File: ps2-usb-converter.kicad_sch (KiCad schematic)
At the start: 1 part, among them J1 Mini-DIN-6

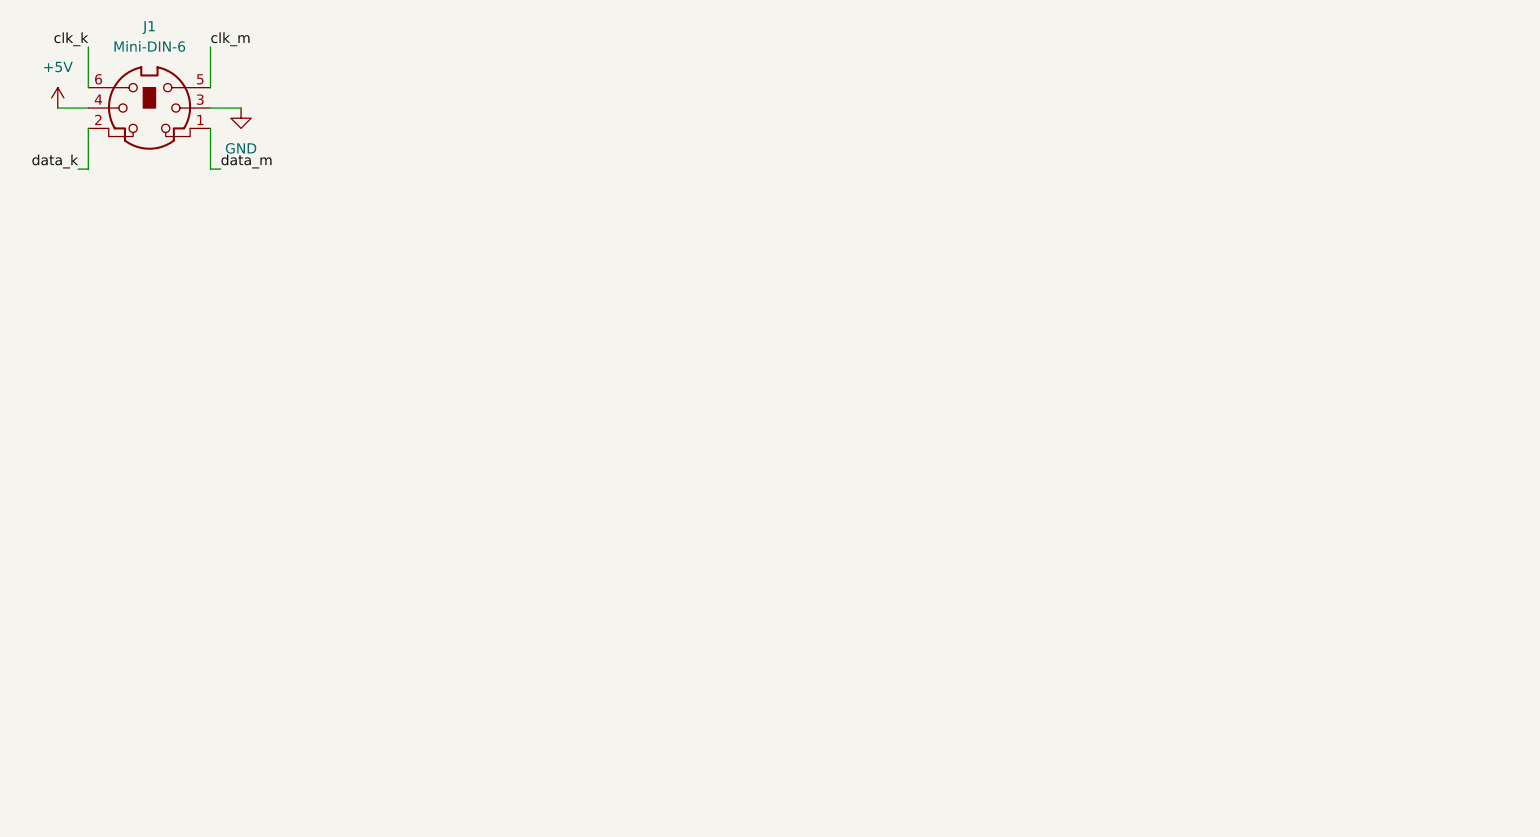
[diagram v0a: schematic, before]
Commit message: Add microcontroller basics and connectors
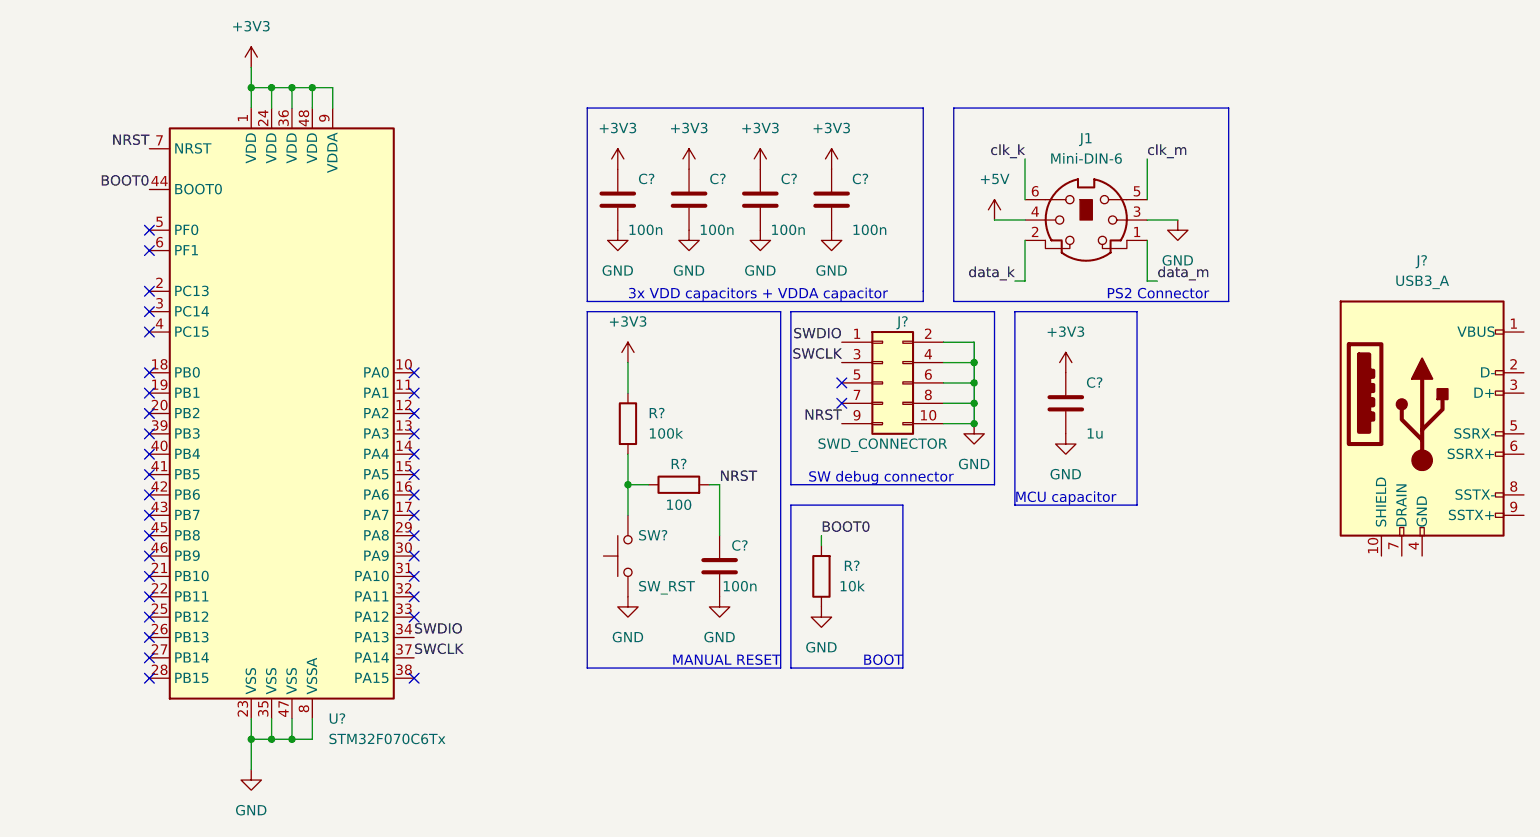
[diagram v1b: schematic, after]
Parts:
- added C? (x5): 100n, Capacitor_SMD:C_0805_2012Metric_Pad1.18x1.45mm_HandSolder, symbol Device:C
- added C?: 1u, Capacitor_SMD:C_0805_2012Metric_Pad1.18x1.45mm_HandSolder, symbol Device:C
- added J?: USB3_A, symbol Connector:USB3_A
- added J?: SWD_CONNECTOR, Connector_PinHeader_2.54mm:PinHeader_2x05_P2.54mm_Vertical, symbol Connector_Generic:Conn_02x05_Odd_Even
- added R?: 10k, Resistor_SMD:R_0805_2012Metric_Pad1.20x1.40mm_HandSolder, symbol Device:R
- added R?: 100, Resistor_SMD:R_0805_2012Metric_Pad1.20x1.40mm_HandSolder, symbol Device:R
- added R?: 100k, Resistor_SMD:R_0805_2012Metric_Pad1.20x1.40mm_HandSolder, symbol Device:R
- added SW?: SW_RST, Button_Switch_SMD:SW_Push_1P1T_NO_6x6mm_H9.5mm, symbol Switch:SW_Push
- added U?: STM32F070C6Tx, Package_QFP:LQFP-48_7x7mm_P0.5mm, symbol MCU_ST_STM32F0:STM32F070C6Tx
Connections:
- net GND: now also C?.2, C?.2, C?.2, C?.2, C?.2, C?.2, J?.10 (Pin_10), J?.2 (Pin_2), J?.4 (Pin_4), J?.6 (Pin_6), J?.8 (Pin_8), R?.1, SW?.1, U?.23 (VSS), U?.35 (VSS), U?.47 (VSS), U?.8 (VSSA)
- new net: R?.1, R?.2, SW?.2
- new net +3V3: C?.1, C?.1, C?.1, C?.1, C?.1, R?.1, U?.1 (VDD), U?.24 (VDD), U?.36 (VDD), U?.48 (VDD), U?.9 (VDDA)
- new net BOOT0: R?.2, U?.44 (BOOT0)
- new net NRST: C?.1, J?.9 (Pin_9), R?.2, U?.7 (NRST)
- new net SWCLK: J?.3 (Pin_3), U?.37 (PA14)
- new net SWDIO: J?.1 (Pin_1), U?.34 (PA13)
- no-connect marks 0 -> 37
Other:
- note added: "3x VDD capacitors + VDDA capacitor"
- note added: "BOOT"
- note added: "MANUAL RESET"
- note added: "MCU capacitor"
- note added: "PS2 Connector"
- note added: "SW debug connector"
- moved on the sheet: J1
